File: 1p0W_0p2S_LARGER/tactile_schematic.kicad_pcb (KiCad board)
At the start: 2 copper layers, 145.2 x 85.6 mm, 55 parts, among them IC1 CY8C4145PVI-PS431, J1 Conn_01x03, J2 Conn_01x04, J3 Conn_01x04, J4 Conn_01x03, J5 Conn_ARM_SWD_TagConnect_TC203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

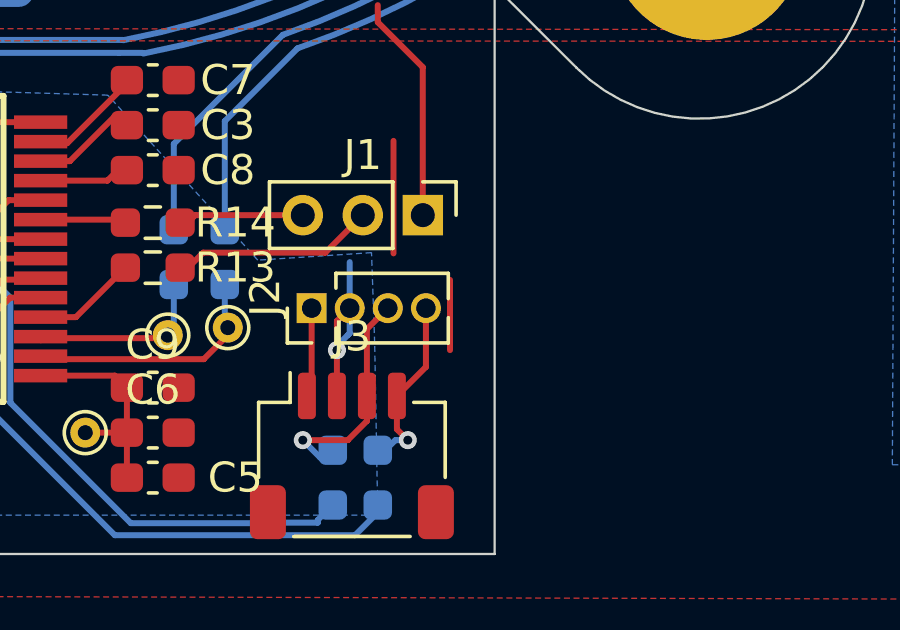
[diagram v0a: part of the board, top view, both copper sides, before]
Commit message: remove redundant gnd trace by scl on larger pcbs
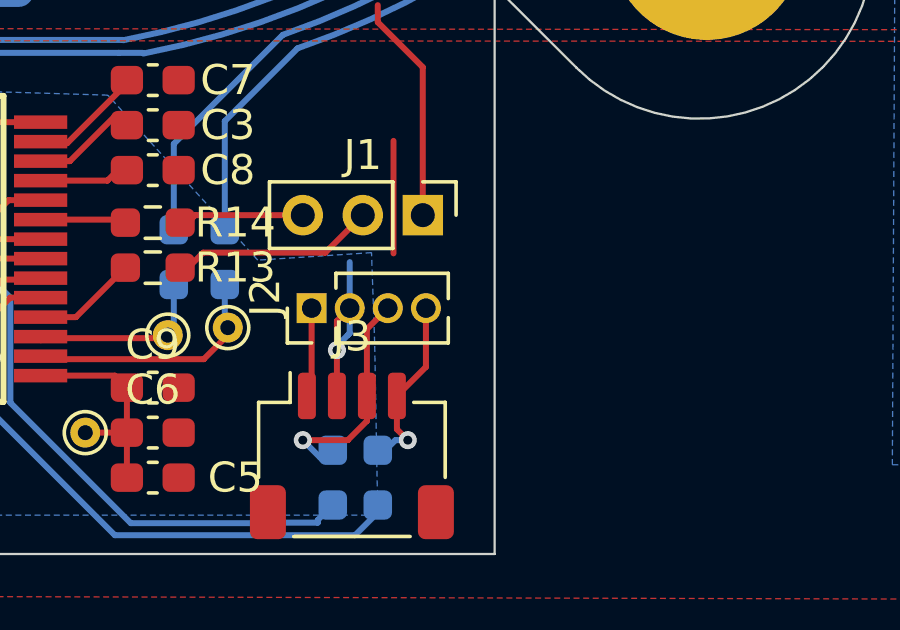
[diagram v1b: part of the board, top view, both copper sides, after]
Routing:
- net GND: track 24.4 -> 22.1 mm
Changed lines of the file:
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@@
 			(psa4output no)
 			(plot_black_and_white yes)
+			(plotinvisibletext no)
 			(sketchpadsonfab no)
 			(plotpadnumbers no)
@@
 		(width 0.2)
 		(layer "F.Cu")
-		(net 2)
-	)
-	(segment
-		(start 131.482849 120.153371)
-		(end 131.482849 122.496125)
-		(width 0.2)
-		(layer "F.Cu")
